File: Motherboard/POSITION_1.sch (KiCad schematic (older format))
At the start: 33 parts, among them Q1 MOSFET_N_(FDMA430NZ), Q2 MOSFET_N_(2N7002P,215), Q3 MOSFET_N_(2N7002P,215), Q4 MOSFET_P_(BS250FTA)

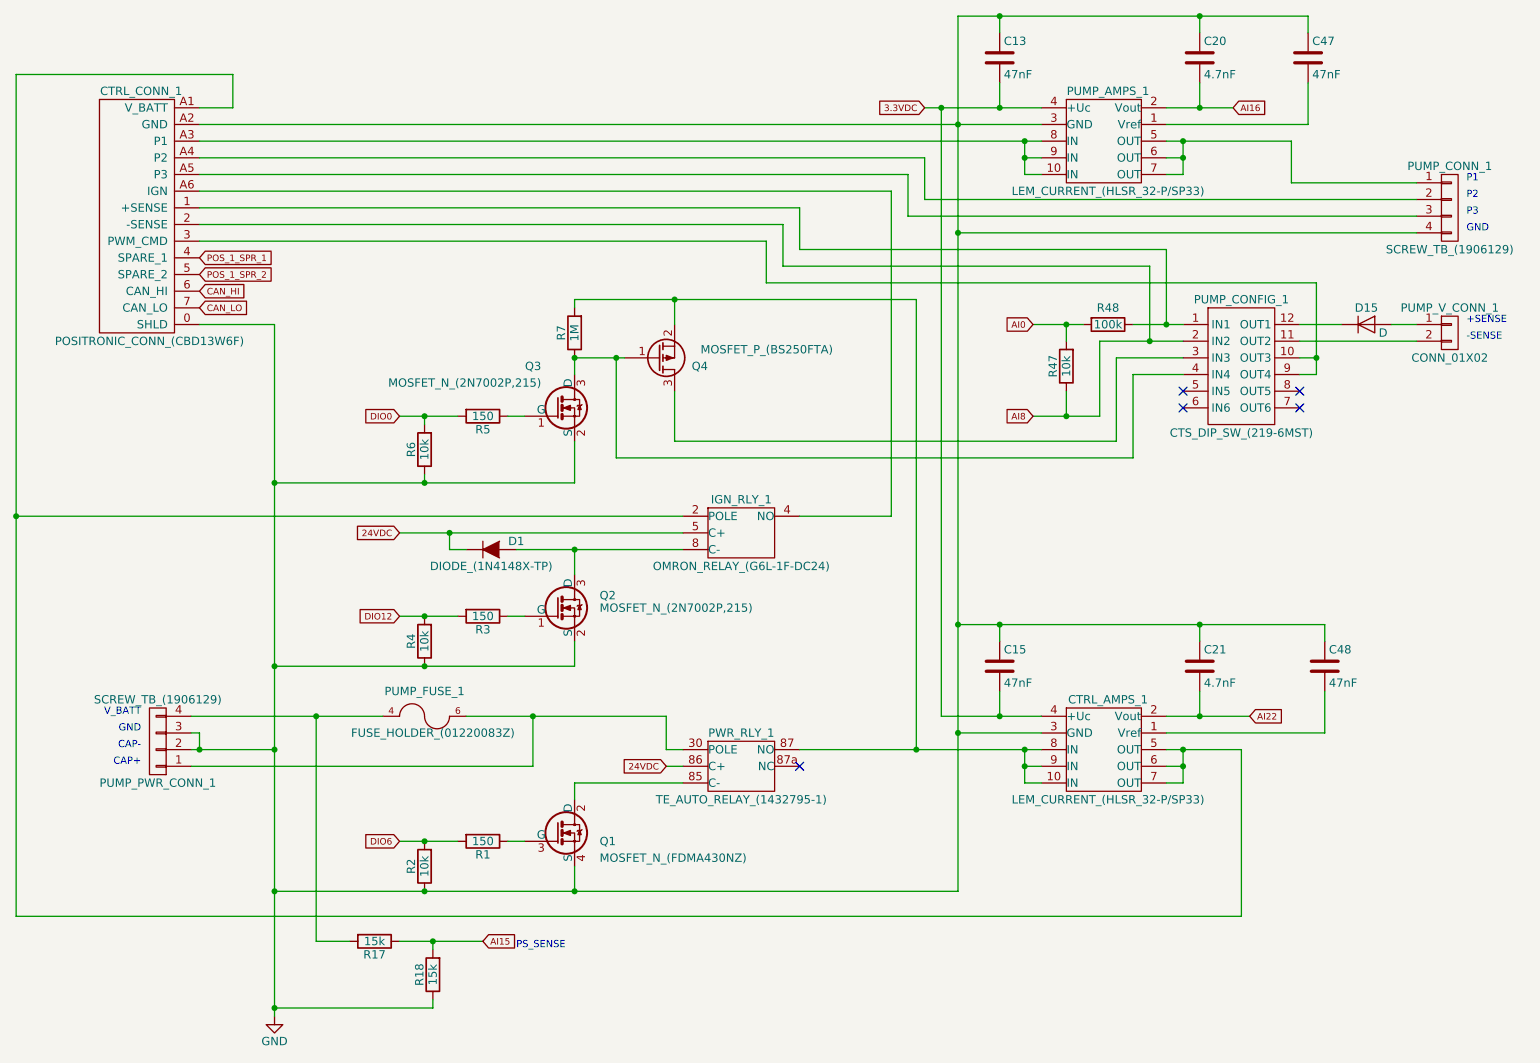
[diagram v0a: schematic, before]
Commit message: - Refer to Google Drive BOM for list of changes for v1.1 - Create drawing for Hella BLDC controller plate.
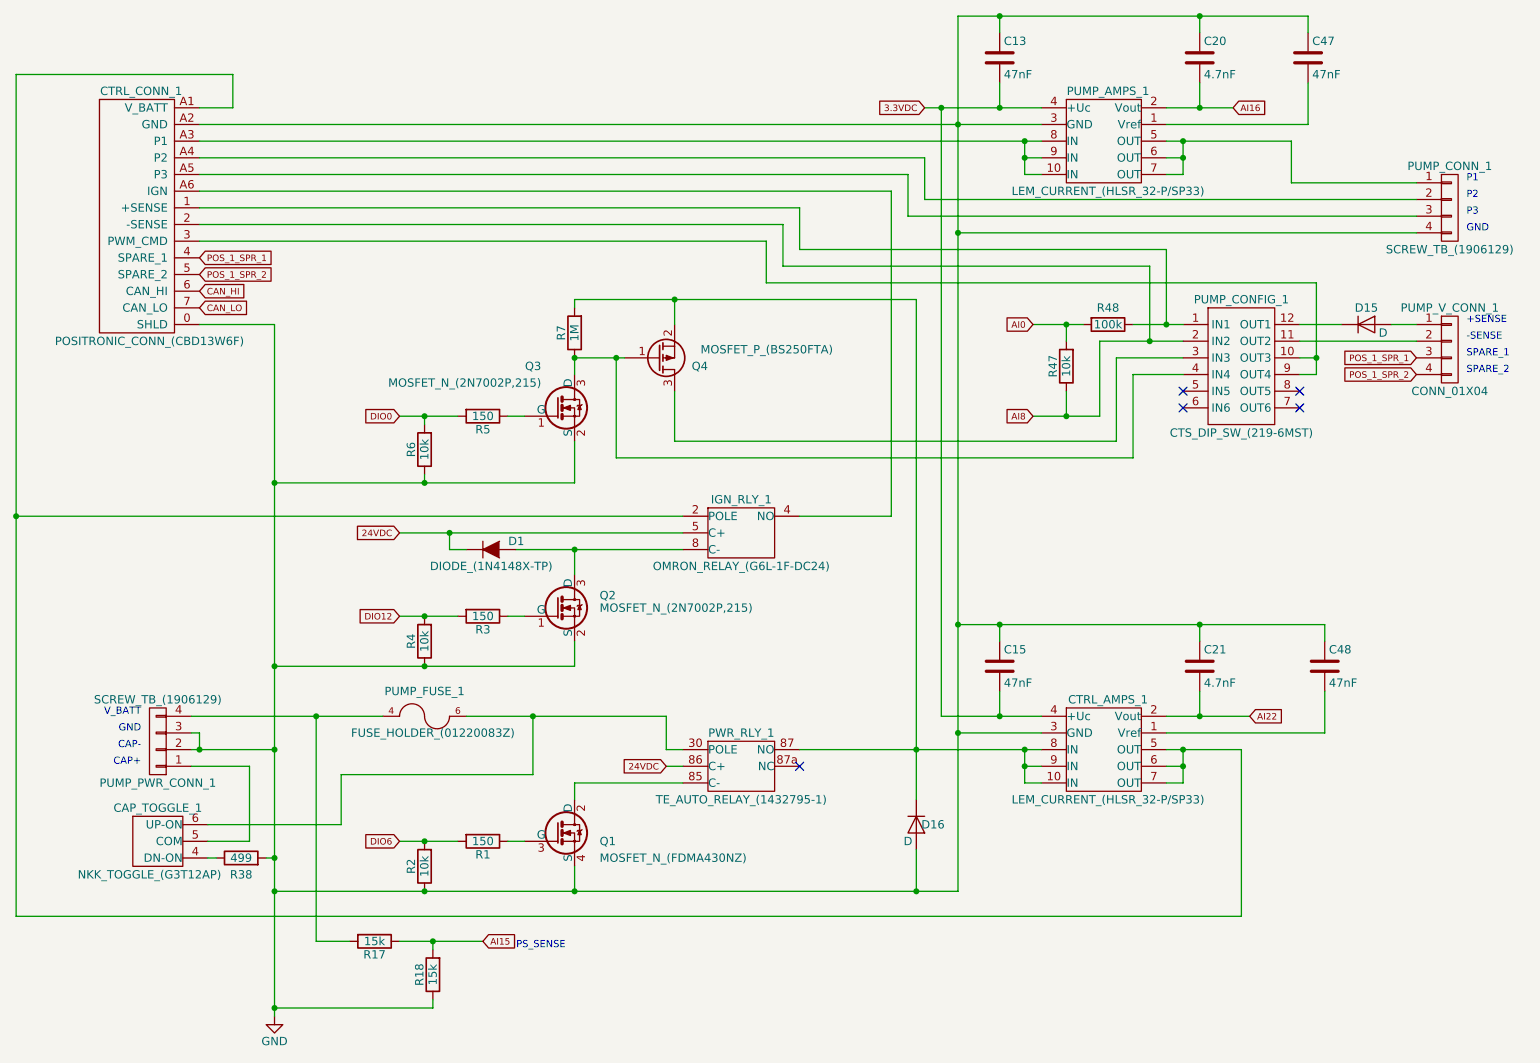
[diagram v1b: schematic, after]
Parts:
- removed PUMP_V_CONN_1: CONN_01X02, Smart_Tank:PHNX_TB_SCREW_2_POS_(1729128), symbol CONN_01X02
- added CAP_TOGGLE_1: NKK_TOGGLE_(G3T12AP), Smart_Tank:NKK_TOGGLE_(G3T12AP), symbol NKK_TOGGLE_(G3T12AP)
- added D16: D, Diodes_SMD:D_SOD-123, symbol D
- added PUMP_V_CONN_1: CONN_01X04, Smart_Tank:PHNX_TB_SCREW_4_POS_(1729144), symbol CONN_01X04
- added R38: 499, Resistors_SMD:R_1206, symbol R
- D15: footprint Diodes_SMD:SOD-523 -> Diodes_SMD:SOD-123
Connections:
- net GND: now also D16.2 (A), R38.2
- net POS_1_SPR_1: now also PUMP_V_CONN_1.3 (P3)
- net POS_1_SPR_2: now also PUMP_V_CONN_1.4 (P4)
- net at PUMP_FUSE_1.6, PUMP_FUSE_1.7, PWR_RLY_1.30 (POLE): now also CAP_TOGGLE_1.6 (UP-ON); no longer PUMP_PWR_CONN_1.1 (P1)
- net at CTRL_AMPS_1.10 (IN), CTRL_AMPS_1.8 (IN), CTRL_AMPS_1.9 (IN)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: now also D16.1 (K)
- net at PUMP_CONFIG_1.11 (OUT2): now also PUMP_V_CONN_1.2 (P2)
- net at D15.2 (A): now also PUMP_V_CONN_1.1 (P1)
- new net: CAP_TOGGLE_1.5 (COM), PUMP_PWR_CONN_1.1 (P1)
- new net: CAP_TOGGLE_1.4 (DN-ON), R38.1
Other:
- note added: "SPARE_1"
- note added: "SPARE_2"

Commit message: - Created Modbus Adapter.
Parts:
- C13, C15, C20, C21, C47, C48: symbol C -> Smart-Tank-Motherboard-rescue:C
- CAP_TOGGLE_1: symbol NKK_TOGGLE_(G3T12AP) -> Smart-Tank-Motherboard-rescue:NKK_TOGGLE_(G3T12AP)
- CTRL_AMPS_1, PUMP_AMPS_1: symbol LEM_CURRENT_(HLSR_32-P/SP33) -> Smart-Tank-Motherboard-rescue:LEM_CURRENT_(HLSR_32-P_SP33)
- CTRL_CONN_1: symbol POSITRONIC_CONN_(CBD13W6F) -> Smart-Tank-Motherboard-rescue:POSITRONIC_CONN_(CBD13W6F)
- D1: symbol DIODE_(1N4148X-TP) -> Smart-Tank-Motherboard-rescue:DIODE_(1N4148X-TP)
- D15, D16: symbol D -> Smart-Tank-Motherboard-rescue:D
- IGN_RLY_1: symbol OMRON_RELAY_(G6L-1F-DC24) -> Smart-Tank-Motherboard-rescue:OMRON_RELAY_(G6L-1F-DC24)
- PUMP_CONFIG_1: symbol CTS_DIP_SW_(219-6MST) -> Smart-Tank-Motherboard-rescue:CTS_DIP_SW_(219-6MST)
- PUMP_CONN_1, PUMP_PWR_CONN_1: symbol SCREW_TB_(1906129) -> Smart-Tank-Motherboard-rescue:SCREW_TB_(1906129)
- PUMP_FUSE_1: symbol FUSE_HOLDER_(01220083Z) -> Smart-Tank-Motherboard-rescue:FUSE_HOLDER_(01220083Z)
- PUMP_V_CONN_1: symbol CONN_01X04 -> Smart-Tank-Motherboard-rescue:CONN_01X04
- PWR_RLY_1: symbol TE_AUTO_RELAY_(1432795-1) -> Smart-Tank-Motherboard-rescue:TE_AUTO_RELAY_(1432795-1)
- Q1: symbol MOSFET_N_(FDMA430NZ) -> Smart-Tank-Motherboard-rescue:MOSFET_N_(FDMA430NZ)
- Q2, Q3: symbol MOSFET_N_(2N7002P,215) -> Smart-Tank-Motherboard-rescue:MOSFET_N_(2N7002P,215)
- Q4: symbol MOSFET_P_(BS250FTA) -> Smart-Tank-Motherboard-rescue:MOSFET_P_(BS250FTA)
- R1, R17, R18, R2, R3, R38, R4, R47, R48, R5, R6, R7: symbol R -> Smart-Tank-Motherboard-rescue:R
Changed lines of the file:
@@
-EESchema Schematic File Version 2
-LIBS:Smart Tank Motherboard-rescue
-LIBS:power
-LIBS:device
-LIBS:transistors
-LIBS:conn
-LIBS:linear
-LIBS:regul
-LIBS:74xx
-LIBS:cmos4000
-LIBS:adc-dac
-LIBS:memory
-LIBS:xilinx
-LIBS:microcontrollers
-LIBS:dsp
-LIBS:microchip
-LIBS:analog_switches
-LIBS:motorola
-LIBS:texas
-LIBS:intel
-LIBS:audio
-LIBS:interface
-LIBS:digital-audio
-LIBS:philips
-LIBS:display
-LIBS:cypress
-LIBS:siliconi
-LIBS:opto
-LIBS:atmel
-LIBS:contrib
-LIBS:valves
+EESchema Schematic File Version 4
 LIBS:Smart Tank Motherboard-cache
-EELAYER 25 0
+EELAYER 29 0
 EELAYER END
 $Descr A4 11693 8268
@@
 $EndDescr
 $Comp
-L R R1
+L Smart-Tank-Motherboard-rescue:R R1
 U 1 1 578929E2
 P 4200 5800
@@
 $EndComp
 $Comp
-L R R2
+L Smart-Tank-Motherboard-rescue:R R2
 U 1 1 578929E9
 P 3850 5950
@@
 $EndComp
 $Comp
-L SCREW_TB_(1906129) PUMP_PWR_CONN_1
+L Smart-Tank-Motherboard-rescue:SCREW_TB_(1906129) PUMP_PWR_CONN_1
 U 1 1 578929F1
 P 2250 5200
@@
 CAP+
 $Comp
-L GND #PWR03
+L Smart-Tank-Motherboard-rescue:GND #PWR03
 U 1 1 578929FC
 P 2950 6850
@@
 $EndComp
 $Comp
-L SCREW_TB_(1906129) PUMP_CONN_1
+L Smart-Tank-Motherboard-rescue:SCREW_TB_(1906129) PUMP_CONN_1
 U 1 1 57892A11
 P 10000 2000
@@
 GND
 $Comp
-L POSITRONIC_CONN_(CBD13W6F) CTRL_CONN_1
+L Smart-Tank-Motherboard-rescue:POSITRONIC_CONN_(CBD13W6F) CTRL_CONN_1
 U 1 1 57892A1C
 P 2150 1950
@@
 $EndComp
 $Comp
-L MOSFET_N_(FDMA430NZ) Q1
+L Smart-Tank-Motherboard-rescue:MOSFET_N_(FDMA430NZ) Q1
 U 1 1 57892A66
 P 4650 5750
@@
 $EndComp
 $Comp
-L TE_AUTO_RELAY_(1432795-1) PWR_RLY_1
+L Smart-Tank-Motherboard-rescue:TE_AUTO_RELAY_(1432795-1) PWR_RLY_1
 U 1 1 57892A6F
 P 5650 5450
@@
 AI22
 $Comp
-L OMRON_RELAY_(G6L-1F-DC24) IGN_RLY_1
+L Smart-Tank-Motherboard-rescue:OMRON_RELAY_(G6L-1F-DC24) IGN_RLY_1
 U 1 1 578975F9
 P 5650 4050
@@
 $EndComp
 $Comp
-L MOSFET_N_(2N7002P,215) Q2
+L Smart-Tank-Motherboard-rescue:MOSFET_N_(2N7002P,215) Q2
 U 1 1 5789B60E
 P 4650 4400
@@
 $EndComp
 $Comp
-L R R3
+L Smart-Tank-Motherboard-rescue:R R3
 U 1 1 5789B766
 P 4200 4450
@@
 $EndComp
 $Comp
-L R R4
+L Smart-Tank-Motherboard-rescue:R R4
 U 1 1 5789B7BF
 P 3850 4600
@@
 CAN_LO
 $Comp
-L DIODE_(1N4148X-TP) D1
+L Smart-Tank-Motherboard-rescue:DIODE_(1N4148X-TP) D1
 U 1 1 578CDC78
 P 4250 4050
@@
 POS_1_SPR_2
 $Comp
-L MOSFET_N_(2N7002P,215) Q3
+L Smart-Tank-Motherboard-rescue:MOSFET_N_(2N7002P,215) Q3
 U 1 1 578D24A7
 P 4650 3200
@@
 $EndComp
 $Comp
-L MOSFET_P_(BS250FTA) Q4
+L Smart-Tank-Motherboard-rescue:MOSFET_P_(BS250FTA) Q4
 U 1 1 578D2B18
 P 5250 2900
@@
 $EndComp
 $Comp
-L R R5
+L Smart-Tank-Motherboard-rescue:R R5
 U 1 1 578D2CB0
 P 4200 3250
@@
 $EndComp
 $Comp
-L R R7
+L Smart-Tank-Motherboard-rescue:R R7
 U 1 1 578D3D02
 P 4750 2750
@@
 DIO0
 $Comp
-L R R6
+L Smart-Tank-Motherboard-rescue:R R6
 U 1 1 578E6CA8
 P 3850 3450
@@
 NoConn ~ 6100 5350
 $Comp
-L R R17
+L Smart-Tank-Motherboard-rescue:R R17
 U 1 1 57976E39
 P 3550 6400
@@
 $EndComp
 $Comp
-L R R18
+L Smart-Tank-Motherboard-rescue:R R18
 U 1 1 57976F71
 P 3900 6600
@@
 PS_SENSE
 $Comp
-L C C20
+L Smart-Tank-Motherboard-rescue:C C20
 U 1 1 579FACCD
 P 8500 1100
@@
 $EndComp
 $Comp
-L C C13
+L Smart-Tank-Motherboard-rescue:C C13
 U 1 1 579FB417
 P 7300 1100
@@
 $EndComp
 $Comp
-L C C21
+L Smart-Tank-Motherboard-rescue:C C21
 U 1 1 579FB9B5
 P 8500 4750
@@
 $EndComp
 $Comp
-L C C15
+L Smart-Tank-Motherboard-rescue:C C15
 U 1 1 579FBB1A
 P 7300 4750
@@
 $EndComp
 $Comp
-L CTS_DIP_SW_(219-6MST) PUMP_CONFIG_1
+L Smart-Tank-Motherboard-rescue:CTS_DIP_SW_(219-6MST) PUMP_CONFIG_1
 U 1 1 57A371C2
 P 8750 2950
@@
 NoConn ~ 8400 3200
 $Comp
-L R R47
+L Smart-Tank-Motherboard-rescue:R R47
 U 1 1 57A392EE
 P 7700 2950
@@
 $EndComp
 $Comp
-L R R48
+L Smart-Tank-Motherboard-rescue:R R48
 U 1 1 57A393A0
 P 7950 2700
@@
 AI8
 $Comp
-L D D15
+L Smart-Tank-Motherboard-rescue:D D15
 U 1 1 57A3F07B
 P 9500 2700
@@
 $EndComp
 $Comp
-L FUSE_HOLDER_(01220083Z) PUMP_FUSE_1
+L Smart-Tank-Motherboard-rescue:FUSE_HOLDER_(01220083Z) PUMP_FUSE_1
 U 1 1 57892A23
 P 3850 5050
@@
 $EndComp
 $Comp
-L LEM_CURRENT_(HLSR_32-P/SP33) PUMP_AMPS_1
+L Smart-Tank-Motherboard-rescue:LEM_CURRENT_(HLSR_32-P_SP33) PUMP_AMPS_1
 U 1 1 57B73648
 P 7800 1600
@@
 $EndComp
 $Comp
-L LEM_CURRENT_(HLSR_32-P/SP33) CTRL_AMPS_1
+L Smart-Tank-Motherboard-rescue:LEM_CURRENT_(HLSR_32-P_SP33) CTRL_AMPS_1
 U 1 1 57B757F3
 P 7800 5250
@@
 $EndComp
 $Comp
-L C C47
+L Smart-Tank-Motherboard-rescue:C C47
 U 1 1 57D1D2CA
 P 9150 1100
@@
 $EndComp
 $Comp
-L C C48
+L Smart-Tank-Motherboard-rescue:C C48
 U 1 1 57D1D80C
 P 9250 4750
@@
 $EndComp
 $Comp
-L NKK_TOGGLE_(G3T12AP) CAP_TOGGLE_1
+L Smart-Tank-Motherboard-rescue:NKK_TOGGLE_(G3T12AP) CAP_TOGGLE_1
 U 1 1 59762F47
 P 2250 5800
@@
 $EndComp
 $Comp
-L D D16
+L Smart-Tank-Motherboard-rescue:D D16
 U 1 1 5976491C
 P 6800 5700
@@
 $EndComp
 $Comp
-L R R38
+L Smart-Tank-Motherboard-rescue:R R38
 U 1 1 59789954
 P 2750 5900
@@
 Connection ~ 2950 5900
 $Comp
-L CONN_01X04 PUMP_V_CONN_1
+L Smart-Tank-Motherboard-rescue:CONN_01X04 PUMP_V_CONN_1
 U 1 1 5979510A
 P 10000 2850
